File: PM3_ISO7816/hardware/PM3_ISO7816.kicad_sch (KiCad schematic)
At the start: 10 parts, among them J1 Smartcard Slot, J2 Conn_01x05, J3 Conn_01x05, U1 N76E003AT20

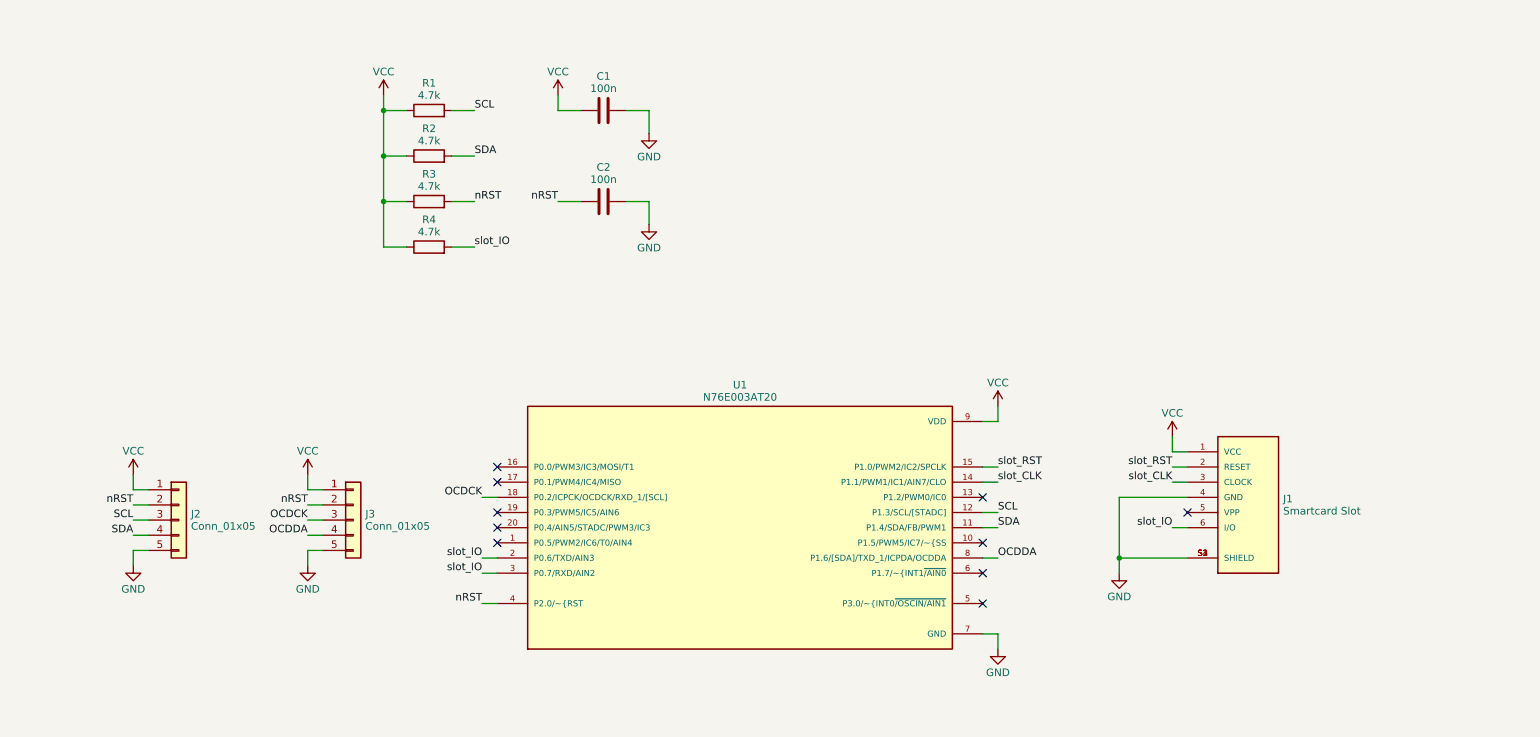
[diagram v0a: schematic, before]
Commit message: Smartcard: Misc work on PCB
Swap VCC pin and GND pin to match the pin order of Nu-Link
Change the footprint of sim card slot for hand soldering
Add test points
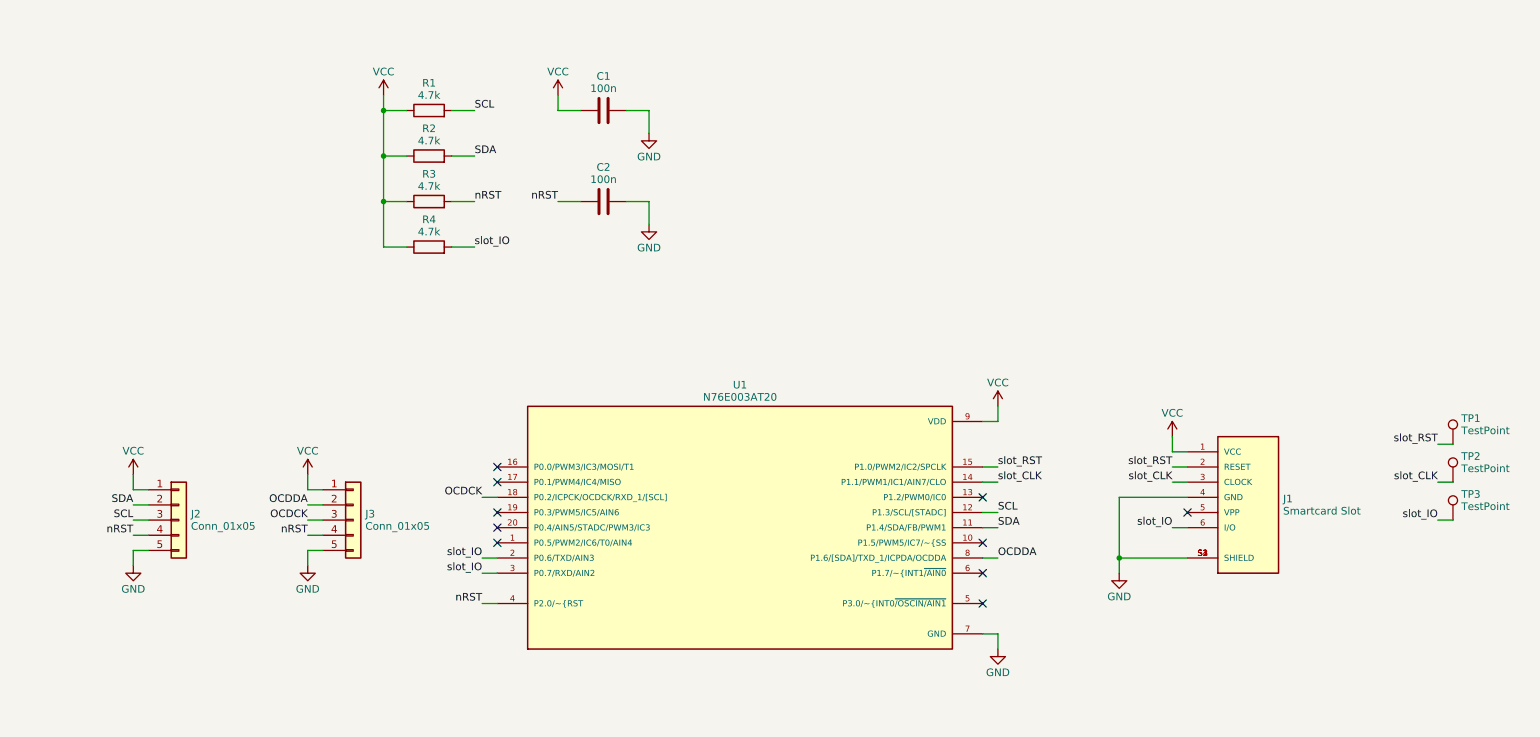
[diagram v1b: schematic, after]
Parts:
- added TP1, TP2, TP3: TestPoint, TestPoint:TestPoint_Pad_D1.0mm, symbol Connector:TestPoint
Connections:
- net OCDDA: now also J3.2 (Pin_2); no longer J3.4 (Pin_4)
- net SDA: now also J2.2 (Pin_2); no longer J2.4 (Pin_4)
- net nRST: now also J2.4 (Pin_4), J3.4 (Pin_4); no longer J2.2 (Pin_2), J3.2 (Pin_2)
- net slot_CLK: now also TP2.1
- net slot_IO: now also TP3.1
- net slot_RST: now also TP1.1
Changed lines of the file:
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@@
+    (stroke (width 0) (type default))
+  )
+  (wire (pts (xy 251.46 91.44) (xy 254 91.44))
     (stroke (width 0) (type default))
   )
@@
     (stroke (width 0) (type default))
   )
+  (wire (pts (xy 251.46 97.79) (xy 254 97.79))
+    (stroke (width 0) (type default))
+  )
   (wire (pts (xy 175.26 104.14) (xy 177.8 104.14))
     (stroke (width 0) (type default))
@@
     (stroke (width 0) (type default))
   )
+  (wire (pts (xy 251.46 85.09) (xy 254 85.09))
+    (stroke (width 0) (type default))
+  )
   (wire (pts (xy 175.26 96.52) (xy 177.8 96.52))
     (stroke (width 0) (type default))
@@
     (stroke (width 0) (type default))
   )
-  (label "nRST" (at 62.23 95.25 180) (fields_autoplaced)
-    (effects (font (size 1.27 1.27)) (justify right bottom))
-  )
   (label "slot_CLK" (at 207.01 91.44 180) (fields_autoplaced)
     (effects (font (size 1.27 1.27)) (justify right bottom))
@@
     (effects (font (size 1.27 1.27)) (justify left bottom))
   )
+  (label "nRST" (at 33.02 100.33 180) (fields_autoplaced)
+    (effects (font (size 1.27 1.27)) (justify right bottom))
+  )
   (label "slot_IO" (at 207.01 99.06 180) (fields_autoplaced)
     (effects (font (size 1.27 1.27)) (justify right bottom))
   )
-  (label "nRST" (at 33.02 95.25 180) (fields_autoplaced)
-    (effects (font (size 1.27 1.27)) (justify right bottom))
-  )
   (label "slot_IO" (at 91.44 104.14 180) (fields_autoplaced)
     (effects (font (size 1.27 1.27)) (justify right bottom))
@@
     (effects (font (size 1.27 1.27)) (justify right bottom))
   )
+  (label "slot_RST" (at 251.46 85.09 180) (fields_autoplaced)
+    (effects (font (size 1.27 1.27)) (justify right bottom))
+  )
   (label "slot_RST" (at 177.8 88.9 0) (fields_autoplaced)
     (effects (font (size 1.27 1.27)) (justify left bottom))
@@
     (effects (font (size 1.27 1.27)) (justify right bottom))
   )
+  (label "nRST" (at 62.23 100.33 180) (fields_autoplaced)
+    (effects (font (size 1.27 1.27)) (justify right bottom))
+  )
+  (label "slot_CLK" (at 251.46 91.44 180) (fields_autoplaced)
+    (effects (font (size 1.27 1.27)) (justify right bottom))
+  )
   (label "nRST" (at 104.14 44.45 180) (fields_autoplaced)
     (effects (font (size 1.27 1.27)) (justify right bottom))
@@
     (effects (font (size 1.27 1.27)) (justify right bottom))
   )
-  (label "OCDDA" (at 62.23 100.33 180) (fields_autoplaced)
+  (label "slot_IO" (at 251.46 97.79 180) (fields_autoplaced)
     (effects (font (size 1.27 1.27)) (justify right bottom))
   )
@@
     (effects (font (size 1.27 1.27)) (justify left bottom))
   )
+  (label "OCDDA" (at 62.23 95.25 180) (fields_autoplaced)
+    (effects (font (size 1.27 1.27)) (justify right bottom))
+  )
   (label "nRST" (at 90.17 44.45 0) (fields_autoplaced)
     (effects (font (size 1.27 1.27)) (justify left bottom))
@@
     (effects (font (size 1.27 1.27)) (justify right bottom))
   )
-  (label "SDA" (at 33.02 100.33 180) (fields_autoplaced)
+  (label "SDA" (at 33.02 95.25 180) (fields_autoplaced)
     (effects (font (size 1.27 1.27)) (justify right bottom))
   )
@@
     )
   )
+  (symbol (lib_id "Connector:TestPoint") (at 254 85.09 0) (unit 1)
+    (in_bom yes) (on_board yes) (dnp no) (fields_autoplaced)
+    (property "Reference" "TP1" (at 255.397 80.764 0)
+      (effects (font (size 1.27 1.27)) (justify left))
+    )
+    (property "Value" "TestPoint" (at 255.397 82.812 0)
+      (effects (font (size 1.27 1.27)) (justify left))
+    )
+    (property "Footprint" "TestPoint:TestPoint_Pad_D1.0mm" (at 259.08 85.09 0)
+      (effects (font (size 1.27 1.27)) hide)
+    )
+    (property "Datasheet" "~" (at 259.08 85.09 0)
+      (effects (font (size 1.27 1.27)) hide)
+    )
+    (pin "1")
+    (instances
+      (project "PM3_ISO7816"
+        (path "/b6fa1ef1-4195-45df-b5c4-9bc1175e0e08"
+          (reference "TP1") (unit 1)
+        )
+      )
+    )
+  )
   (symbol (lib_id "Device:R") (at 82.55 36.83 90) (unit 1)
     (in_bom yes) (on_board yes) (dnp no) (fields_autoplaced)
@@
   )
   (symbol (lib_id "Connector_Generic:Conn_01x05") (at 40.64 97.79 0) (unit 1)
-    (in_bom yes) (on_board yes) (dnp no) (fields_autoplaced)
+    (in_bom yes) (on_board yes) (dnp no)
     (property "Reference" "J2" (at 42.672 96.766 0)
       (effects (font (size 1.27 1.27)) (justify left))
@@
     )
   )
+  (symbol (lib_id "Connector:TestPoint") (at 254 91.44 0) (unit 1)
+    (in_bom yes) (on_board yes) (dnp no) (fields_autoplaced)
+    (property "Reference" "TP2" (at 255.397 87.114 0)
+      (effects (font (size 1.27 1.27)) (justify left))
+    )
+    (property "Value" "TestPoint" (at 255.397 89.162 0)
+      (effects (font (size 1.27 1.27)) (justify left))
+    )
+    (property "Footprint" "TestPoint:TestPoint_Pad_D1.0mm" (at 259.08 91.44 0)
+      (effects (font (size 1.27 1.27)) hide)
+    )
+    (property "Datasheet" "~" (at 259.08 91.44 0)
+      (effects (font (size 1.27 1.27)) hide)
+    )
+    (pin "1")
+    (instances
+      (project "PM3_ISO7816"
+        (path "/b6fa1ef1-4195-45df-b5c4-9bc1175e0e08"
+          (reference "TP2") (unit 1)
+        )
+      )
+    )
+  )
   (symbol (lib_id "power:VCC") (at 74.93 26.67 0) (unit 1)
     (in_bom yes) (on_board yes) (dnp no) (fields_autoplaced)
@@
         )
       )
+    )
+  )
+  (symbol (lib_id "Connector:TestPoint") (at 254 97.79 0) (unit 1)
+    (in_bom yes) (on_board yes) (dnp no) (fields_autoplaced)
+    (property "Reference" "TP3" (at 255.397 93.464 0)
+      (effects (font (size 1.27 1.27)) (justify left))
+    )
+    (property "Value" "TestPoint" (at 255.397 95.512 0)
+      (effects (font (size 1.27 1.27)) (justify left))
+    )
+    (property "Footprint" "TestPoint:TestPoint_Pad_D1.0mm" (at 259.08 97.79 0)
+      (effects (font (size 1.27 1.27)) hide)
+    )
+    (property "Datasheet" "~" (at 259.08 97.79 0)
+      (effects (font (size 1.27 1.27)) hide)
+    )
+    (pin "1")
+    (instances
+      (project "PM3_ISO7816"
+        (path "/b6fa1ef1-4195-45df-b5c4-9bc1175e0e08"
+          (reference "TP3") (unit 1)
+        )
+      )

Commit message: Add schematic pdf
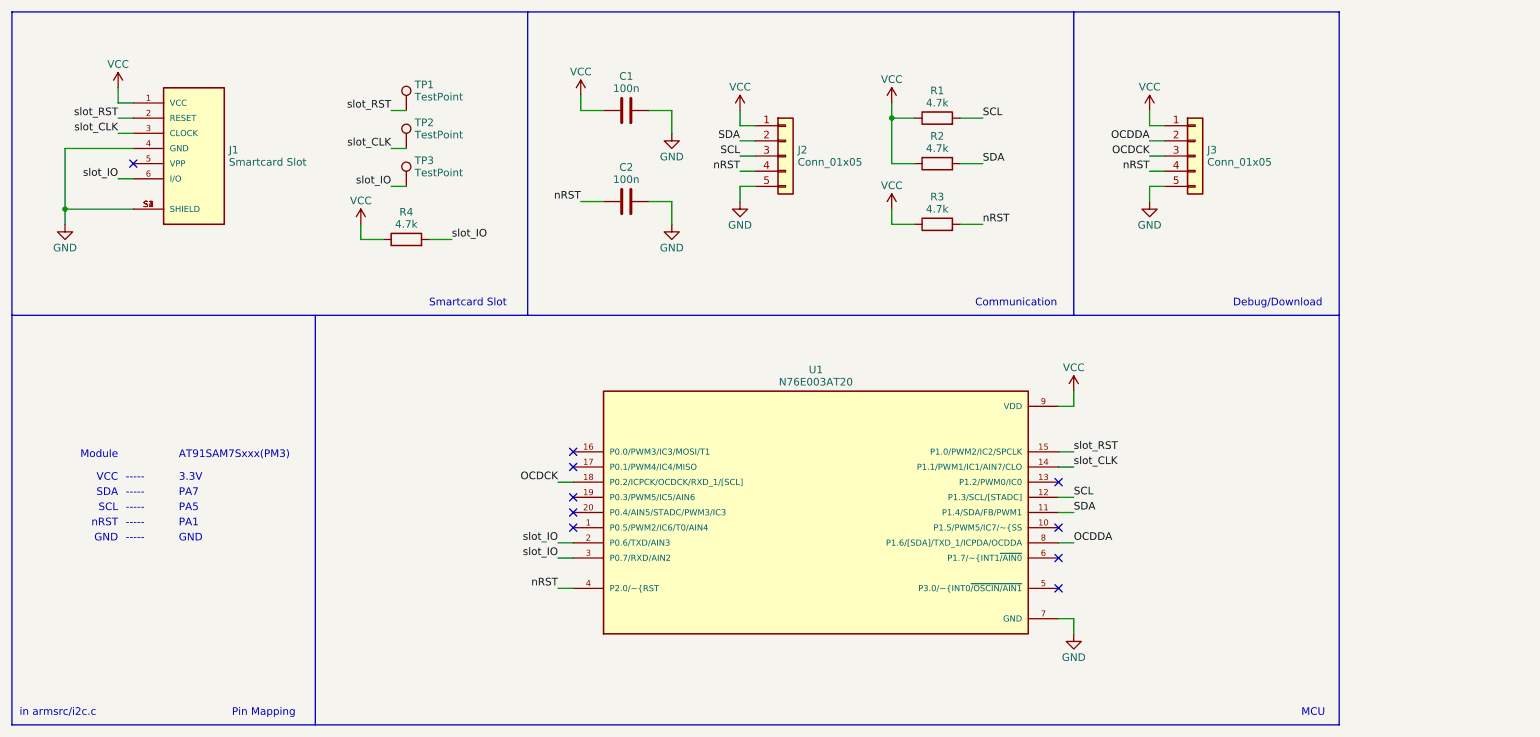
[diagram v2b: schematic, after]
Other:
- note added: "-----"
- note added: "3.3V"
- note added: "AT91SAM7Sxxx(PM3)"
- note added: "Communication"
- note added: "Debug/Download"
- note added: "GND"
- note added: "MCU"
- note added: "Module"
- note added: "PA1"
- note added: "PA5"
- note added: "PA7"
- note added: "Pin Mapping"
- note added: "SCL"
- note added: "SDA"
- note added: "Smartcard Slot"
- note added: "VCC"
- note added: "in armsrc/i2c.c"
- note added: "nRST"
- moved on the sheet: C1, C2, J1, J2, J3, R1, R2, R3, R4, TP1, TP2, TP3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
